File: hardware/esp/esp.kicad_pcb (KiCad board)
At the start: 2 copper layers, 100 x 80 mm, 90 parts, among them J1 Conn_01x02, J2 USB_C_Receptacle_USB2.0_16P, J3 USB_C_Receptacle_USB2.0_16P, J4 Conn_01x02, J5 Conn_Coaxial, J6 Conn_01x09_Pin, J7 Conn_01x06_Pin, J8 Conn_01x09_Pin, SW1 RESET, SW2 BOOT, U1 AMS1117-3.3, U2 CP2102N-Axx-xQFN20, U3 ESP32-S3-WROOM-1, U4 VL53L0X, U5 NRF24L01, U6 BME280, Y1 16MHz

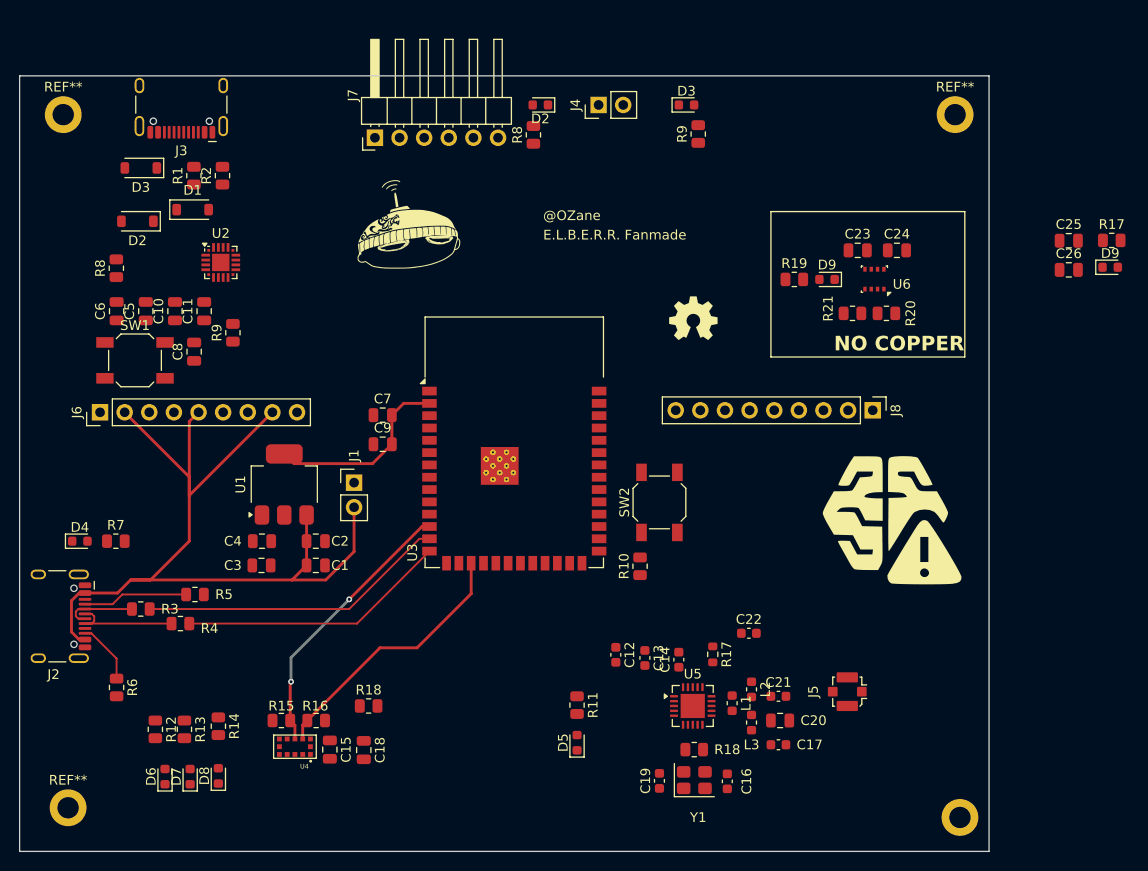
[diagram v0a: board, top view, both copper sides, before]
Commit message: Fixing schematic error and routing PCB
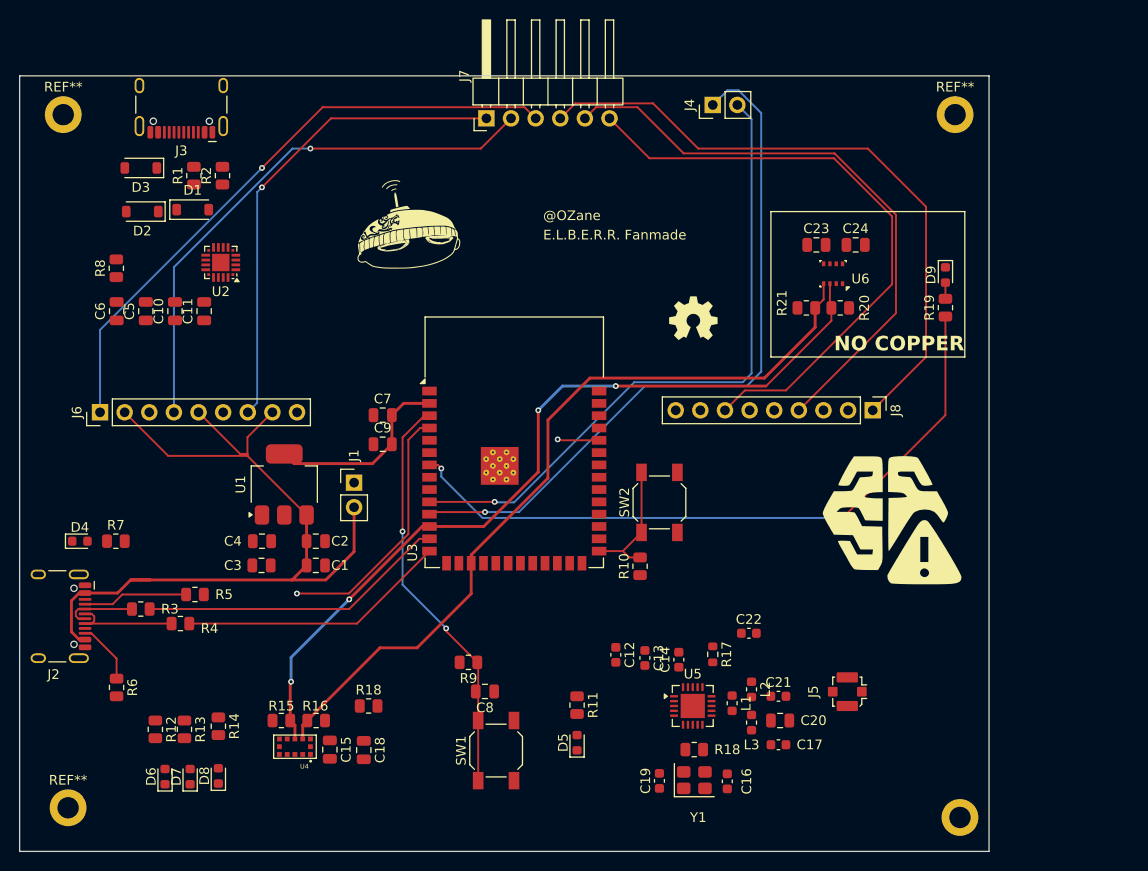
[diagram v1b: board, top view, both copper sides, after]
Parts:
- removed C25, C26: C, Capacitor_SMD:C_0805_2012Metric
- removed the D2 at (138.7, 73.0)
- removed the D3 at (153.8, 73.0)
- removed the D9 at (197.5, 89.7)
- removed the R17 at (197.7, 87.0)
- removed the R8 at (138.0, 76.1)
- removed the R9 at (155.0, 76.0)
- moved SW1 54.8 mm to (134.1, 139.6), turned to 90 degrees
- moved C8 46.1 mm to (133.0, 133.5), turned to 180 degrees
- moved R9 41.8 mm to (131.3, 130.5), turned to 180 degrees
- moved R19 15.9 mm to (180.5, 93.9), turned to 90 degrees
- moved D9 12.2 mm to (180.5, 90.5), turned to -90 degrees
- moved J4 11.8 mm to (156.5, 73.0)
- moved J7 11.7 mm to (133.2, 74.4)
- moved R20 4.80 mm to (169.7, 93.9)
- moved R21 4.80 mm to (166.2, 93.9)
- moved U6 4.30 mm to (168.9, 90.4)
- moved C23 4.30 mm to (167.2, 87.4)
- moved C24 4.30 mm to (171.2, 87.4)
- moved D2 1.12 mm to (97.7, 84.0)
- turned U2 to 180 degrees
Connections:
- C5 pad 2: unconnected-(C5-Pad2) -> GND
- J7 pad 6: RH -> RP
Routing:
- net RX2: track 0.00 -> 73.6 mm, vias 0 -> 1
- net TEMP_LED: track 0.00 -> 70.6 mm, vias 0 -> 2
- net TX2: track 0.00 -> 67.1 mm, vias 0 -> 1
- net RH: track 0.00 -> 66.1 mm
- net LH: track 0.00 -> 63.4 mm, vias 0 -> 1
- net RP: track 0.00 -> 63.0 mm
- net RV: track 0.00 -> 61.5 mm
- net SDA: track 28.5 -> 86.4 mm, vias 2 -> 4
- net LV: track 0.00 -> 56.1 mm, vias 0 -> 1
- net SCL: track 27.6 -> 82.0 mm
- net LP: track 0.00 -> 49.9 mm, vias 0 -> 1
- net EN: track 0.00 -> 42.3 mm, vias 0 -> 2
- net NF.SKULL: track 0.00 -> 26.6 mm, vias 0 -> 1
- net BOOT: track 0.00 -> 13.4 mm
- net +5V: track 93.0 -> 85.7 mm
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
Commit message: Updating PCB
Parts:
- moved R13 3.91 mm to (105.9, 137.4)
- moved D7 3.58 mm to (106.0, 141.2)
- moved D8 3.07 mm to (102.6, 141.2)
- moved R14 2.92 mm to (102.6, 137.4)
- moved D6 1.47 mm to (99.0, 141.2)
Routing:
- net +3V3: track 19.7 -> 36.0 mm, vias 0 -> 1
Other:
- board text added: "CLOSED"
- board text added: "FLOATING"
- board text added: "OPENED"
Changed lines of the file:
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@@
 	(footprint "Resistor_SMD:R_0805_2012Metric"
 		(layer "F.Cu")
-		(at 102 137.4125 -90)
+		(at 105.909999 137.4125 -90)
 		(descr "Resistor SMD 0805 (2012 Metric), square (rectangular) end terminal, IPC-7351 nominal, (Body size source: IPC-SM-782 page 72, https://www.pcb-3d.com/wordpress/wp-content/uploads/ipc-sm-782a_amendment_1_and_2.pdf)")
 		(tags "resistor")
@@
 	(footprint "LED_SMD:LED_0603_1608Metric"
 		(layer "F.Cu")
-		(at 102.590001 142.287501 90)
+		(at 106 141.212499 90)
 		(descr "LED SMD 0603 (1608 Metric), square (rectangular) end terminal, IPC-7351 nominal, (Body size source: http://www.tortai-tech.com/upload/download/2011102023233369053.pdf)")
 		(tags "LED")
@@
 	(footprint "LED_SMD:LED_0603_1608Metric"
 		(layer "F.Cu")
-		(at 100 142.287501 90)
+		(at 99 141.212499 90)
 		(descr "LED SMD 0603 (1608 Metric), square (rectangular) end terminal, IPC-7351 nominal, (Body size source: http://www.tortai-tech.com/upload/download/2011102023233369053.pdf)")
 		(tags "LED")
@@
 		)
 		(property "Value" "LED"
-			(at 3.287501 -0.5 90)
+			(at 0.287501 -3.5 90)
 			(layer "F.Fab")
 			(effects
@@
 	(footprint "Resistor_SMD:R_0805_2012Metric"
 		(layer "F.Cu")
-		(at 105.5 137.0875 -90)
+		(at 102.6 137.3875 -90)
 		(descr "Resistor SMD 0805 (2012 Metric), square (rectangular) end terminal, IPC-7351 nominal, (Body size source: IPC-SM-782 page 72, https://www.pcb-3d.com/wordpress/wp-content/uploads/ipc-sm-782a_amendment_1_and_2.pdf)")
 		(tags "resistor")
@@
 	(footprint "LED_SMD:LED_0603_1608Metric"
 		(layer "F.Cu")
-		(at 105.5 142.212499 90)
+		(at 102.6 141.212499 90)
 		(descr "LED SMD 0603 (1608 Metric), square (rectangular) end terminal, IPC-7351 nominal, (Body size source: http://www.tortai-tech.com/upload/download/2011102023233369053.pdf)")
 		(tags "LED")
@@
 		(layer "Edge.Cuts")
 	)
+	(gr_text "OPENED"
+		(at 99.5 147.424998 90)
+		(layer "F.SilkS")
+		(effects
+			(font
+				(size 0.7 0.7)
+				(thickness 0.08)
+			)
+			(justify left bottom)
+		)
+	)
+	(gr_text "FLOATING"
+		(at 103 147.924998 90)
+		(layer "F.SilkS")
+		(effects
+			(font
+				(size 0.7 0.7)
+				(thickness 0.08)
+			)
+			(justify left bottom)
+		)
+	)
+	(gr_text "CLOSED"
+		(at 106.5 147.424998 90)
+		(layer "F.SilkS")
+		(effects
+			(font
+				(size 0.7 0.7)
+				(thickness 0.08)
+			)
+			(justify left bottom)
+		)
+	)
 	(gr_text "NO COPPER"
 		(at 169 98.5 0)
@@
 	)
 	(segment
+		(start 110.899998 118.5)
+		(end 110.899998 120.5)
+		(width 0.2)
+		(layer "F.Cu")
+		(net "+3V3")
+	)
+	(segment
+		(start 110.949999 118)
+		(end 110.949999 118.449999)
+		(width 0.2)
+		(layer "F.Cu")
+		(net "+3V3")
+	)
+	(segment
+		(start 115 138.4)
+		(end 116.849999 138.4)
+		(width 0.2)
+		(layer "F.Cu")
+		(net "+3V3")
+	)
+	(segment
+		(start 110.899998 120.5)
+		(end 111.740378 121.34038)
+		(width 0.2)
+		(layer "F.Cu")
+		(net "+3V3")
+	)
+	(segment
 		(start 124.615 103.785)
 		(end 127.275 103.785)
@@
 	)
 	(segment
+		(start 111.740378 121.34038)
+		(end 112.84038 121.34038)
+		(width 0.2)
+		(layer "F.Cu")
+		(net "+3V3")
+	)
+	(segment
 		(start 123.4 105)
 		(end 124.615 103.785)
@@
 	)
 	(segment
+		(start 116.849999 138.4)
+		(end 117 138.550001)
+		(width 0.2)
+		(layer "F.Cu")
+		(net "+3V3")
+	)
+	(segment
+		(start 112.3 115.299998)
+		(end 112.3 116.649999)
+		(width 0.2)
+		(layer "F.Cu")
+		(net "+3V3")
+	)
+	(segment
+		(start 115.550001 140)
+		(end 117 138.550001)
+		(width 0.2)
+		(layer "F.Cu")
+		(net "+3V3")
+	)
+	(segment
+		(start 115 140)
+		(end 115.550001 140)
+		(width 0.2)
+		(layer "F.Cu")
+		(net "+3V3")
+	)
+	(segment
 		(start 123.4 108)
 		(end 123.4 105)
@@
 		(net "+3V3")
 	)
+	(segment
+		(start 110.949999 118.449999)
+		(end 110.899998 118.5)
+		(width 0.2)
+		(layer "F.Cu")
+		(net "+3V3")
+	)
+	(segment
+		(start 112.3 116.649999)
+		(end 110.949999 118)
+		(width 0.2)
+		(layer "F.Cu")
+		(net "+3V3")
+	)
+	(segment
+		(start 117 138.550001)
+		(end 120.449999 138.550001)
+		(width 0.2)
+		(layer "F.Cu")
+		(net "+3V3")
+	)
+	(segment
+		(start 120.449999 138.550001)
+		(end 120.5 138.600002)
+		(width 0.2)
+		(layer "F.Cu")
+		(net "+3V3")
+	)
+	(via
+		(at 112.84038 121.34038)
+		(size 0.6)
+		(drill 0.3)
+		(layers "F.Cu" "B.Cu")
+		(net "+3V3")
+	)

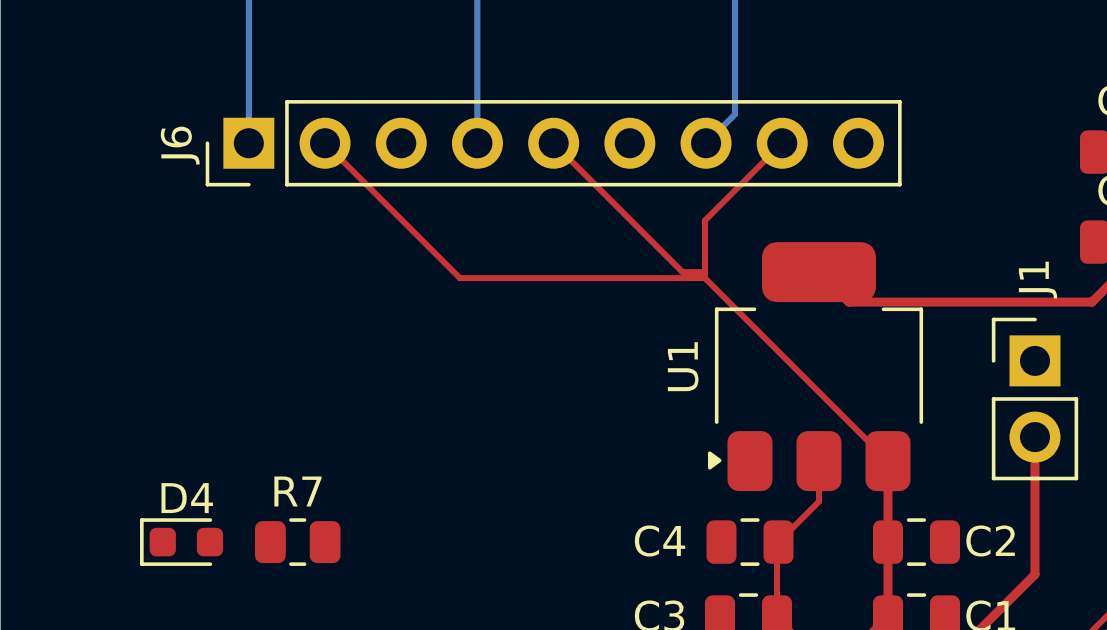
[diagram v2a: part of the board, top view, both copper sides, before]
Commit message: Modifiying schematic after schematic review
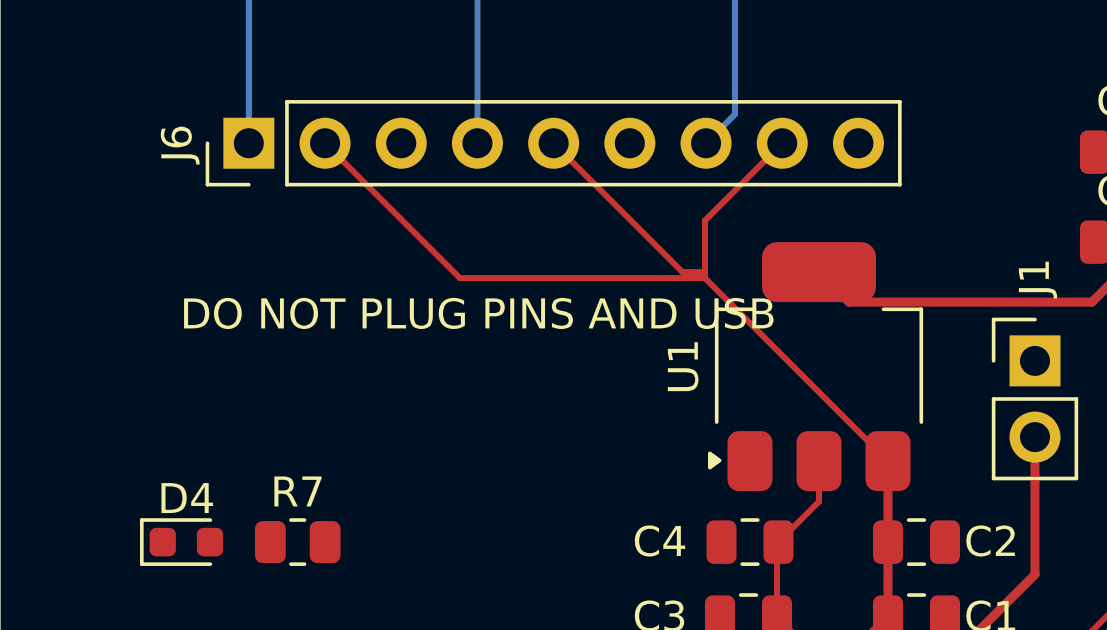
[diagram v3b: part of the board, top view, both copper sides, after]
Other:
- board text added: "DO NOT PLUG PINS AND USB"
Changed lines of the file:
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@@
+		)
+	)
+	(gr_text "DO NOT PLUG PINS AND USB "
+		(at 91 111 0)
+		(layer "F.SilkS")
+		(effects
+			(font
+				(size 1 1)
+				(thickness 0.1)
+			)
+			(justify left bottom)
 		)
 	)
@@
 	)
 	(segment
-		(start 180.5 91.325)
-		(end 180.5 93)
-		(width 0.2)
-		(layer "F.Cu")
-		(net "Net-(D9-A)")
-	)
-	(segment
 		(start 144.775 119.025)
 		(end 147.224999 119.025)
@@
 	)
 	(segment
+		(start 180.5 91.325)
+		(end 180.5 93)
+		(width 0.2)
+		(layer "F.Cu")
+		(net "Net-(D9-A)")
+	)
+	(segment

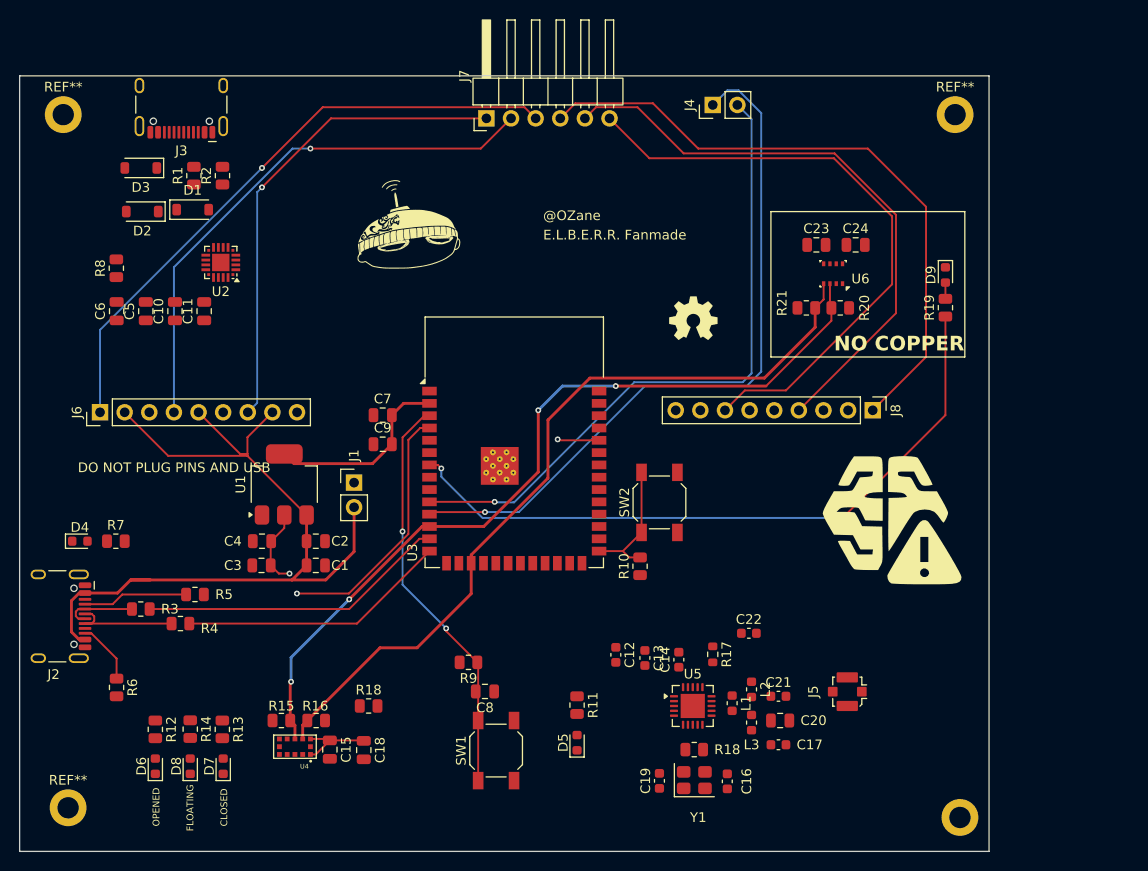
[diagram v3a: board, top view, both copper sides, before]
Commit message: Updating schemaitc, and component placement on PCB
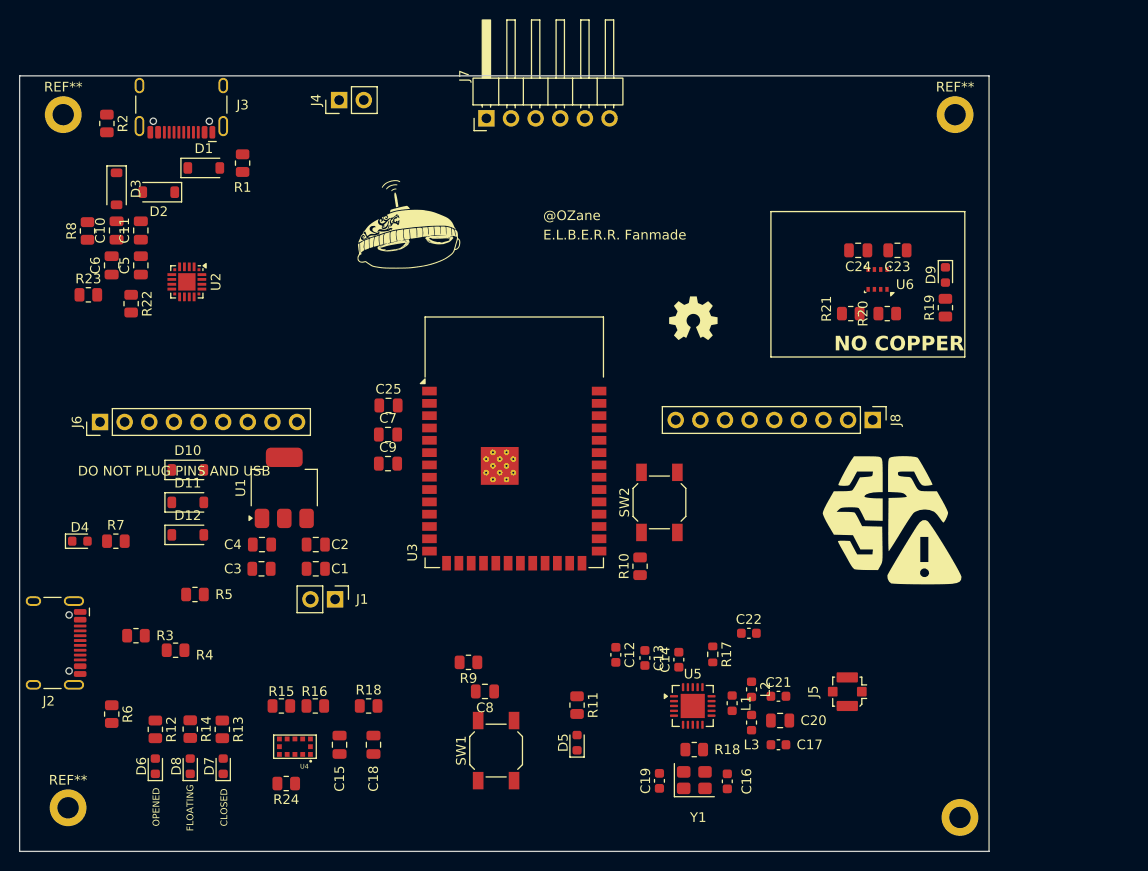
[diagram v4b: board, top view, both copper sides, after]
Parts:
- added C25: 0.1uF, Capacitor_SMD:C_0805_2012Metric, F.Cu at (123.0, 104.0)
- added D10: D_TVS, Diode_SMD:D_SOD-123, F.Cu at (102.3, 110.7)
- added D11: D_TVS, Diode_SMD:D_SOD-123, F.Cu at (102.3, 114.0)
- added D12: D_TVS, Diode_SMD:D_SOD-123, F.Cu at (102.3, 117.3)
- added R22: 47.5k, Resistor_SMD:R_0805_2012Metric, F.Cu at (96.5, 93.5)
- added R23: 22.1k, Resistor_SMD:R_0805_2012Metric, F.Cu at (92.1, 92.6)
- added R24: 10k, Resistor_SMD:R_0805_2012Metric, F.Cu at (112.5, 143.0)
- C15: value 100nF -> 0.1uF
- C17: value 2.2pF -> 2.2nF
- C18: value 4.7pF -> 4.7uF
- C7: value 100uF -> 10uF
- L2: value 2.7nH -> 3.9nH
- L3: value 3.9nH -> 2.7nH
- R8: value 4.7k -> 1k
- moved J4 38.5 mm to (118.0, 72.5)
- moved R2 13.1 mm to (94.0, 74.9), turned to -90 degrees
- moved J1 12.2 mm to (117.5, 124.0), turned to -90 degrees
- moved C11 10.6 mm to (97.5, 85.9)
- moved C10 10.3 mm to (95.0, 85.9)
- moved C23 8.38 mm to (175.6, 88.0), turned to 180 degrees
- moved R1 5.19 mm to (108.0, 79.0), turned to -90 degrees
- moved R20 4.89 mm to (174.5, 94.5), turned to 0 degrees
- moved R8 4.86 mm to (92.0, 86.0)
- moved C5 4.75 mm to (97.5, 89.6)
- moved C6 4.75 mm to (94.5, 89.6)
- moved R21 4.62 mm to (170.7, 94.5)
- moved U6 4.62 mm to (173.5, 91.0)
- moved D1 4.45 mm to (104.0, 79.5)
- moved U2 4.03 mm to (102.2, 91.2), turned to -90 degrees
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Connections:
- C10 pad 1: +3V3 -> /VDD
- C11 pad 1: +3V3 -> /VDD
- R20 pad 1: +3V3 -> SDA
- R20 pad 2: SDA -> +3V3
- R8 pad 1: +3V3 -> /VDD
- U2 pad 6: +3V3 -> /VDD
- U2 pad 8: Net-(D3-A1) -> Net-(U2-VBUS)
- U4 pad 5: +3V3 -> Net-(U4-~{XSHUT})
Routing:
- net SDA: track 86.4 -> 0.00 mm, vias 4 -> 0
- net +5V: track 85.7 -> 0.00 mm
- net SCL: track 82.0 -> 0.00 mm
- net RX2: track 73.6 -> 0.00 mm, vias 1 -> 0
- net TEMP_LED: track 70.6 -> 0.00 mm, vias 2 -> 0
- net TX2: track 67.1 -> 0.00 mm, vias 1 -> 0
- net RH: track 66.1 -> 0.00 mm
- net LH: track 63.4 -> 0.00 mm, vias 1 -> 0
- net RP: track 63.0 -> 0.00 mm
- net RV: track 61.5 -> 0.00 mm
- net LV: track 56.1 -> 0.00 mm, vias 1 -> 0
- net LP: track 49.9 -> 0.00 mm, vias 1 -> 0
- net EN: track 42.3 -> 0.00 mm, vias 2 -> 0
- net +3V3: track 36.0 -> 0.00 mm, vias 1 -> 0
- net D-: track 31.9 -> 0.00 mm
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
